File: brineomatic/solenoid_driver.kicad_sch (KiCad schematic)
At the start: 8 parts, among them J6 3.5MM, J7 3.5MM, Q1 AO3400A

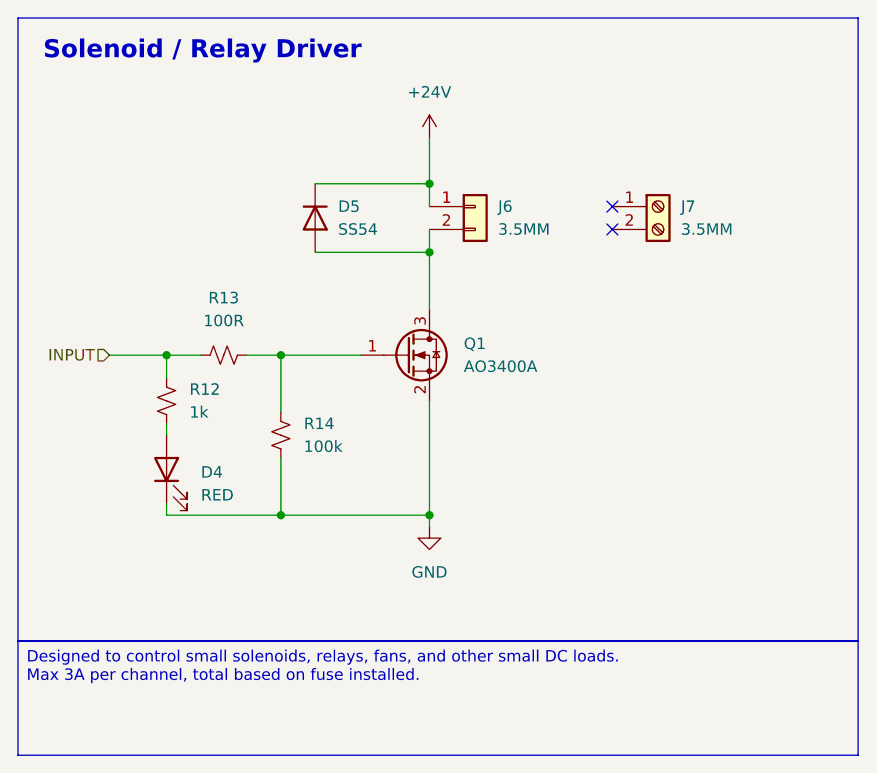
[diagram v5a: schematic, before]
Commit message: added pullup resistor to adc alert
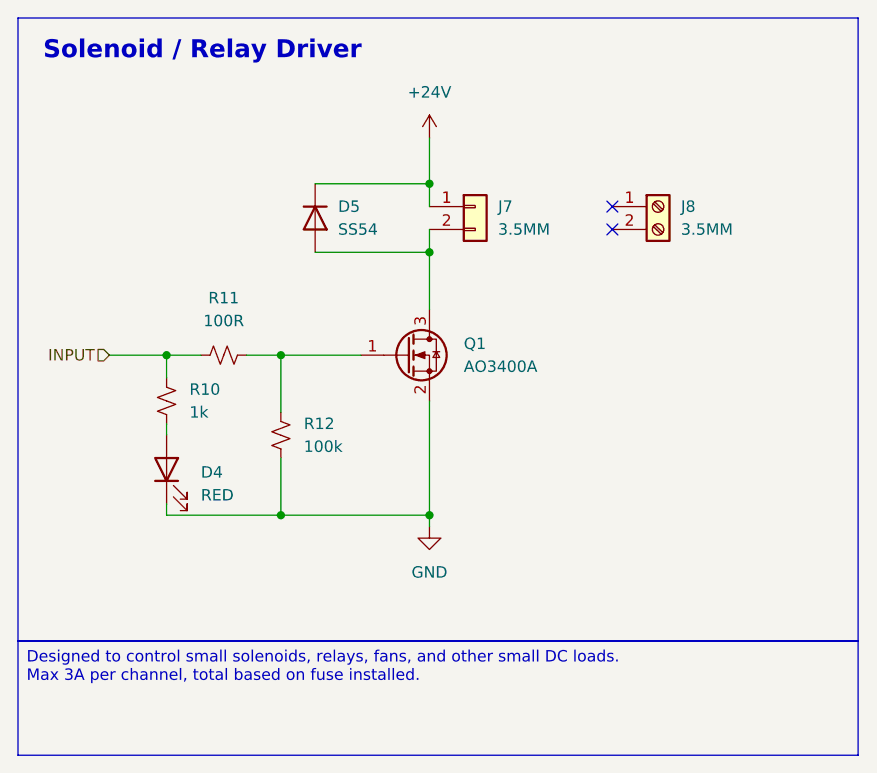
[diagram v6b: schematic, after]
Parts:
- renumbered J6 to J7, J7 to J8, R12 to R10, R13 to R11, R14 to R12
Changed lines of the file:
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@@
 		(dnp no)
 		(fields_autoplaced yes)
-		(property "Reference" "J7"
+		(property "Reference" "J8"
 			(at 166.37 72.3899 0)
 			(effects
@@
 			(project ""
 				(path "/96477ae2-ef08-48f3-8dd4-fe4478541f68/427089b2-03f8-442f-beb9-df87f2c31083"
-					(reference "J14")
-					(unit 1)
-				)
-				(path "/96477ae2-ef08-48f3-8dd4-fe4478541f68/91db2587-0f96-4292-982e-c9eb44a28398"
-					(reference "J7")
-					(unit 1)
-				)
-				(path "/96477ae2-ef08-48f3-8dd4-fe4478541f68/c855463c-7233-4758-aee4-aa81e2b08bc2"
-					(reference "J12")
-					(unit 1)
-				)
-				(path "/96477ae2-ef08-48f3-8dd4-fe4478541f68/dbb171ac-9e75-41dd-9596-6fac72a797a4"
-					(reference "J16")
+					(reference "J15")
+					(unit 1)
+				)
+				(path "/96477ae2-ef08-48f3-8dd4-fe4478541f68/91db2587-0f96-4292-982e-c9eb44a28398"
+					(reference "J8")
+					(unit 1)
+				)
+				(path "/96477ae2-ef08-48f3-8dd4-fe4478541f68/c855463c-7233-4758-aee4-aa81e2b08bc2"
+					(reference "J13")
+					(unit 1)
+				)
+				(path "/96477ae2-ef08-48f3-8dd4-fe4478541f68/dbb171ac-9e75-41dd-9596-6fac72a797a4"
+					(reference "J17")
 					(unit 1)
 				)
@@
 		(dnp no)
 		(fields_autoplaced yes)
-		(property "Reference" "#PWR020"
+		(property "Reference" "#PWR022"
 			(at 138.43 114.3 0)
 			(effects
@@
 			(project "brineomatic"
 				(path "/96477ae2-ef08-48f3-8dd4-fe4478541f68/427089b2-03f8-442f-beb9-df87f2c31083"
+					(reference "#PWR038")
+					(unit 1)
+				)
+				(path "/96477ae2-ef08-48f3-8dd4-fe4478541f68/91db2587-0f96-4292-982e-c9eb44a28398"
+					(reference "#PWR022")
+					(unit 1)
+				)
+				(path "/96477ae2-ef08-48f3-8dd4-fe4478541f68/c855463c-7233-4758-aee4-aa81e2b08bc2"
 					(reference "#PWR036")
 					(unit 1)
 				)
-				(path "/96477ae2-ef08-48f3-8dd4-fe4478541f68/91db2587-0f96-4292-982e-c9eb44a28398"
-					(reference "#PWR020")
-					(unit 1)
-				)
-				(path "/96477ae2-ef08-48f3-8dd4-fe4478541f68/c855463c-7233-4758-aee4-aa81e2b08bc2"
-					(reference "#PWR034")
-					(unit 1)
-				)
-				(path "/96477ae2-ef08-48f3-8dd4-fe4478541f68/dbb171ac-9e75-41dd-9596-6fac72a797a4"
-					(reference "#PWR038")
+				(path "/96477ae2-ef08-48f3-8dd4-fe4478541f68/dbb171ac-9e75-41dd-9596-6fac72a797a4"
+					(reference "#PWR040")
 					(unit 1)
 				)
@@
 		(dnp no)
 		(fields_autoplaced yes)
-		(property "Reference" "R12"
+		(property "Reference" "R10"
 			(at 111.76 92.7099 0)
 			(effects
@@
 				)
 				(path "/96477ae2-ef08-48f3-8dd4-fe4478541f68/91db2587-0f96-4292-982e-c9eb44a28398"
-					(reference "R12")
+					(reference "R10")
 					(unit 1)
 				)
@@
 		(dnp no)
 		(fields_autoplaced yes)
-		(property "Reference" "R13"
+		(property "Reference" "R11"
 			(at 115.57 82.55 90)
 			(effects
@@
 				)
 				(path "/96477ae2-ef08-48f3-8dd4-fe4478541f68/91db2587-0f96-4292-982e-c9eb44a28398"
-					(reference "R13")
+					(reference "R11")
 					(unit 1)
 				)
@@
 		(dnp no)
 		(fields_autoplaced yes)
-		(property "Reference" "J6"
+		(property "Reference" "J7"
 			(at 146.05 72.3899 0)
 			(effects
@@
 			(project "brineomatic"
 				(path "/96477ae2-ef08-48f3-8dd4-fe4478541f68/427089b2-03f8-442f-beb9-df87f2c31083"
-					(reference "J13")
-					(unit 1)
-				)
-				(path "/96477ae2-ef08-48f3-8dd4-fe4478541f68/91db2587-0f96-4292-982e-c9eb44a28398"
-					(reference "J6")
-					(unit 1)
-				)
-				(path "/96477ae2-ef08-48f3-8dd4-fe4478541f68/c855463c-7233-4758-aee4-aa81e2b08bc2"
-					(reference "J11")
-					(unit 1)
-				)
-				(path "/96477ae2-ef08-48f3-8dd4-fe4478541f68/dbb171ac-9e75-41dd-9596-6fac72a797a4"
-					(reference "J15")
+					(reference "J14")
+					(unit 1)
+				)
+				(path "/96477ae2-ef08-48f3-8dd4-fe4478541f68/91db2587-0f96-4292-982e-c9eb44a28398"
+					(reference "J7")
+					(unit 1)
+				)
+				(path "/96477ae2-ef08-48f3-8dd4-fe4478541f68/c855463c-7233-4758-aee4-aa81e2b08bc2"
+					(reference "J12")
+					(unit 1)
+				)
+				(path "/96477ae2-ef08-48f3-8dd4-fe4478541f68/dbb171ac-9e75-41dd-9596-6fac72a797a4"
+					(reference "J16")
 					(unit 1)
 				)
@@
 		(dnp no)
 		(fields_autoplaced yes)
-		(property "Reference" "R14"
+		(property "Reference" "R12"
 			(at 124.46 96.5199 0)
 			(effects
@@
 				)
 				(path "/96477ae2-ef08-48f3-8dd4-fe4478541f68/91db2587-0f96-4292-982e-c9eb44a28398"
-					(reference "R14")
+					(reference "R12")
 					(unit 1)
 				)
@@
 		(dnp no)
 		(fields_autoplaced yes)
-		(property "Reference" "#PWR019"
+		(property "Reference" "#PWR021"
 			(at 138.43 68.58 0)
 			(effects
@@
 			(project "brineomatic"
 				(path "/96477ae2-ef08-48f3-8dd4-fe4478541f68/427089b2-03f8-442f-beb9-df87f2c31083"
+					(reference "#PWR037")
+					(unit 1)
+				)
+				(path "/96477ae2-ef08-48f3-8dd4-fe4478541f68/91db2587-0f96-4292-982e-c9eb44a28398"
+					(reference "#PWR021")
+					(unit 1)
+				)
+				(path "/96477ae2-ef08-48f3-8dd4-fe4478541f68/c855463c-7233-4758-aee4-aa81e2b08bc2"
 					(reference "#PWR035")
 					(unit 1)
 				)
-				(path "/96477ae2-ef08-48f3-8dd4-fe4478541f68/91db2587-0f96-4292-982e-c9eb44a28398"
-					(reference "#PWR019")
-					(unit 1)
-				)
-				(path "/96477ae2-ef08-48f3-8dd4-fe4478541f68/c855463c-7233-4758-aee4-aa81e2b08bc2"
-					(reference "#PWR033")
-					(unit 1)
-				)
-				(path "/96477ae2-ef08-48f3-8dd4-fe4478541f68/dbb171ac-9e75-41dd-9596-6fac72a797a4"
-					(reference "#PWR037")
-					(unit 1)
-				)
+				(path "/96477ae2-ef08-48f3-8dd4-fe4478541f68/dbb171ac-9e75-41dd-9596-6fac72a797a4"
+					(reference "#PWR039")
+					(unit 1)
+				)

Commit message: changed mosfet pulldowns to 10k. moved 5v to esp32_5v to power everything over usb.
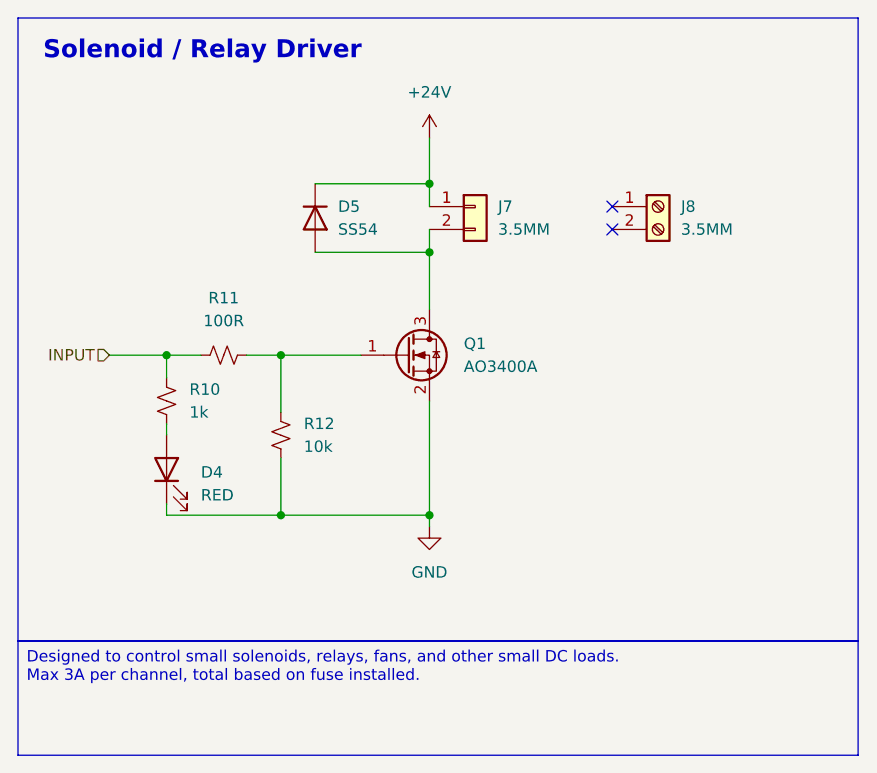
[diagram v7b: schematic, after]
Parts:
- R12: value 100k -> 10k
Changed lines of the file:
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@@
 			)
 		)
-		(property "Value" "100k"
+		(property "Value" "10k"
 			(at 124.46 99.0599 0)
 			(effects

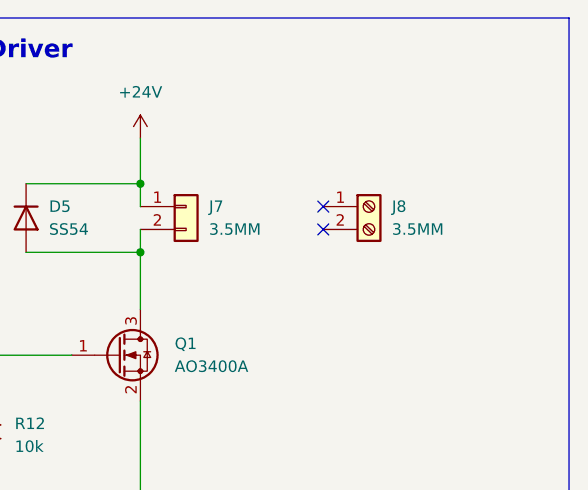
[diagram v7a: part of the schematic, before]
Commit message: stacked tds, removed stepper vref, pulled in esp32-s3 schematic, added extra relay output
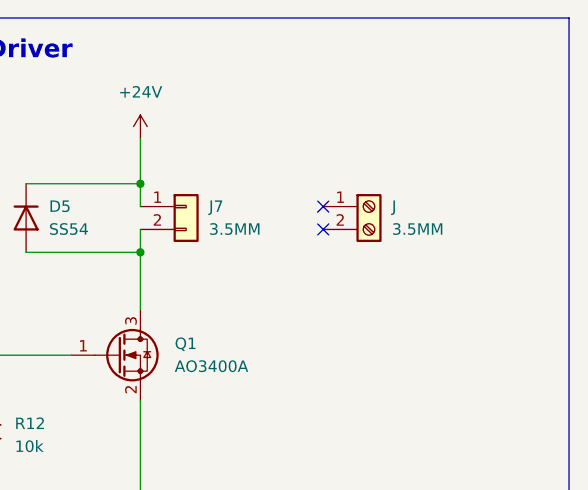
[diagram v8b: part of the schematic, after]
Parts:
- renumbered J8 to J
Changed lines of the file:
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@@
+					(unit 1)
+				)
+				(path "/96477ae2-ef08-48f3-8dd4-fe4478541f68/53b9b350-c996-44b6-8dbf-2a99841f1965"
+					(reference "D?")
 					(unit 1)
 				)
@@
 		(dnp no)
 		(fields_autoplaced yes)
-		(property "Reference" "J8"
+		(property "Reference" "J"
 			(at 166.37 72.3899 0)
 			(effects
@@
 		)
 		(instances
-			(project ""
-				(path "/96477ae2-ef08-48f3-8dd4-fe4478541f68/427089b2-03f8-442f-beb9-df87f2c31083"
-					(reference "J15")
-					(unit 1)
-				)
-				(path "/96477ae2-ef08-48f3-8dd4-fe4478541f68/91db2587-0f96-4292-982e-c9eb44a28398"
-					(reference "J8")
-					(unit 1)
-				)
-				(path "/96477ae2-ef08-48f3-8dd4-fe4478541f68/c855463c-7233-4758-aee4-aa81e2b08bc2"
-					(reference "J13")
-					(unit 1)
-				)
-				(path "/96477ae2-ef08-48f3-8dd4-fe4478541f68/dbb171ac-9e75-41dd-9596-6fac72a797a4"
-					(reference "J17")
+			(project "brineomatic"
+				(path "/96477ae2-ef08-48f3-8dd4-fe4478541f68/53b9b350-c996-44b6-8dbf-2a99841f1965"
+					(reference "J?")
 					(unit 1)
 				)
@@
 			(project "brineomatic"
 				(path "/96477ae2-ef08-48f3-8dd4-fe4478541f68/427089b2-03f8-442f-beb9-df87f2c31083"
-					(reference "#PWR038")
+					(reference "#PWR037")
+					(unit 1)
+				)
+				(path "/96477ae2-ef08-48f3-8dd4-fe4478541f68/53b9b350-c996-44b6-8dbf-2a99841f1965"
+					(reference "#PWR068")
 					(unit 1)
 				)
@@
 				)
 				(path "/96477ae2-ef08-48f3-8dd4-fe4478541f68/c855463c-7233-4758-aee4-aa81e2b08bc2"
-					(reference "#PWR036")
+					(reference "#PWR035")
 					(unit 1)
 				)
 				(path "/96477ae2-ef08-48f3-8dd4-fe4478541f68/dbb171ac-9e75-41dd-9596-6fac72a797a4"
-					(reference "#PWR040")
+					(reference "#PWR039")
 					(unit 1)
 				)
@@
 					(unit 1)
 				)
+				(path "/96477ae2-ef08-48f3-8dd4-fe4478541f68/53b9b350-c996-44b6-8dbf-2a99841f1965"
+					(reference "R?")
+					(unit 1)
+				)
 				(path "/96477ae2-ef08-48f3-8dd4-fe4478541f68/91db2587-0f96-4292-982e-c9eb44a28398"
 					(reference "R10")
@@
 					(unit 1)
 				)
+				(path "/96477ae2-ef08-48f3-8dd4-fe4478541f68/53b9b350-c996-44b6-8dbf-2a99841f1965"
+					(reference "R?")
+					(unit 1)
+				)
 				(path "/96477ae2-ef08-48f3-8dd4-fe4478541f68/91db2587-0f96-4292-982e-c9eb44a28398"
 					(reference "R11")
@@
 					(unit 1)
 				)
+				(path "/96477ae2-ef08-48f3-8dd4-fe4478541f68/53b9b350-c996-44b6-8dbf-2a99841f1965"
+					(reference "J?")
+					(unit 1)
+				)
 				(path "/96477ae2-ef08-48f3-8dd4-fe4478541f68/91db2587-0f96-4292-982e-c9eb44a28398"
 					(reference "J7")
@@
 					(unit 1)
 				)
+				(path "/96477ae2-ef08-48f3-8dd4-fe4478541f68/53b9b350-c996-44b6-8dbf-2a99841f1965"
+					(reference "R?")
+					(unit 1)
+				)
 				(path "/96477ae2-ef08-48f3-8dd4-fe4478541f68/91db2587-0f96-4292-982e-c9eb44a28398"
 					(reference "R12")
@@
 					(unit 1)
 				)
+				(path "/96477ae2-ef08-48f3-8dd4-fe4478541f68/53b9b350-c996-44b6-8dbf-2a99841f1965"
+					(reference "Q?")
+					(unit 1)
+				)
 				(path "/96477ae2-ef08-48f3-8dd4-fe4478541f68/91db2587-0f96-4292-982e-c9eb44a28398"
 					(reference "Q1")
@@
 			(project "brineomatic"
 				(path "/96477ae2-ef08-48f3-8dd4-fe4478541f68/427089b2-03f8-442f-beb9-df87f2c31083"
-					(reference "#PWR037")
+					(reference "#PWR036")
+					(unit 1)
+				)
+				(path "/96477ae2-ef08-48f3-8dd4-fe4478541f68/53b9b350-c996-44b6-8dbf-2a99841f1965"
+					(reference "#PWR067")
 					(unit 1)
 				)
@@
 				)
 				(path "/96477ae2-ef08-48f3-8dd4-fe4478541f68/c855463c-7233-4758-aee4-aa81e2b08bc2"
-					(reference "#PWR035")
+					(reference "#PWR034")
 					(unit 1)
 				)
 				(path "/96477ae2-ef08-48f3-8dd4-fe4478541f68/dbb171ac-9e75-41dd-9596-6fac72a797a4"
-					(reference "#PWR039")
+					(reference "#PWR038")
 					(unit 1)
 				)
@@
 					(unit 1)
 				)
+				(path "/96477ae2-ef08-48f3-8dd4-fe4478541f68/53b9b350-c996-44b6-8dbf-2a99841f1965"
+					(reference "D?")
+					(unit 1)
+				)
